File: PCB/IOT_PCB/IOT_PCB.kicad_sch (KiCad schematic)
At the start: 19 parts, among them J1 Screw_Terminal_01x02, J2 Screw_Terminal_01x02, J3 10155435-00011LF USB-C, U1 ESP32-S3-MINI-1, U2 BME280, U3 SCD41-D-R2, U4 ENS160-BGLM, U5 AMS1117-3.3, U6 AMS1117-1.8, U7 USBLC6-2SC6

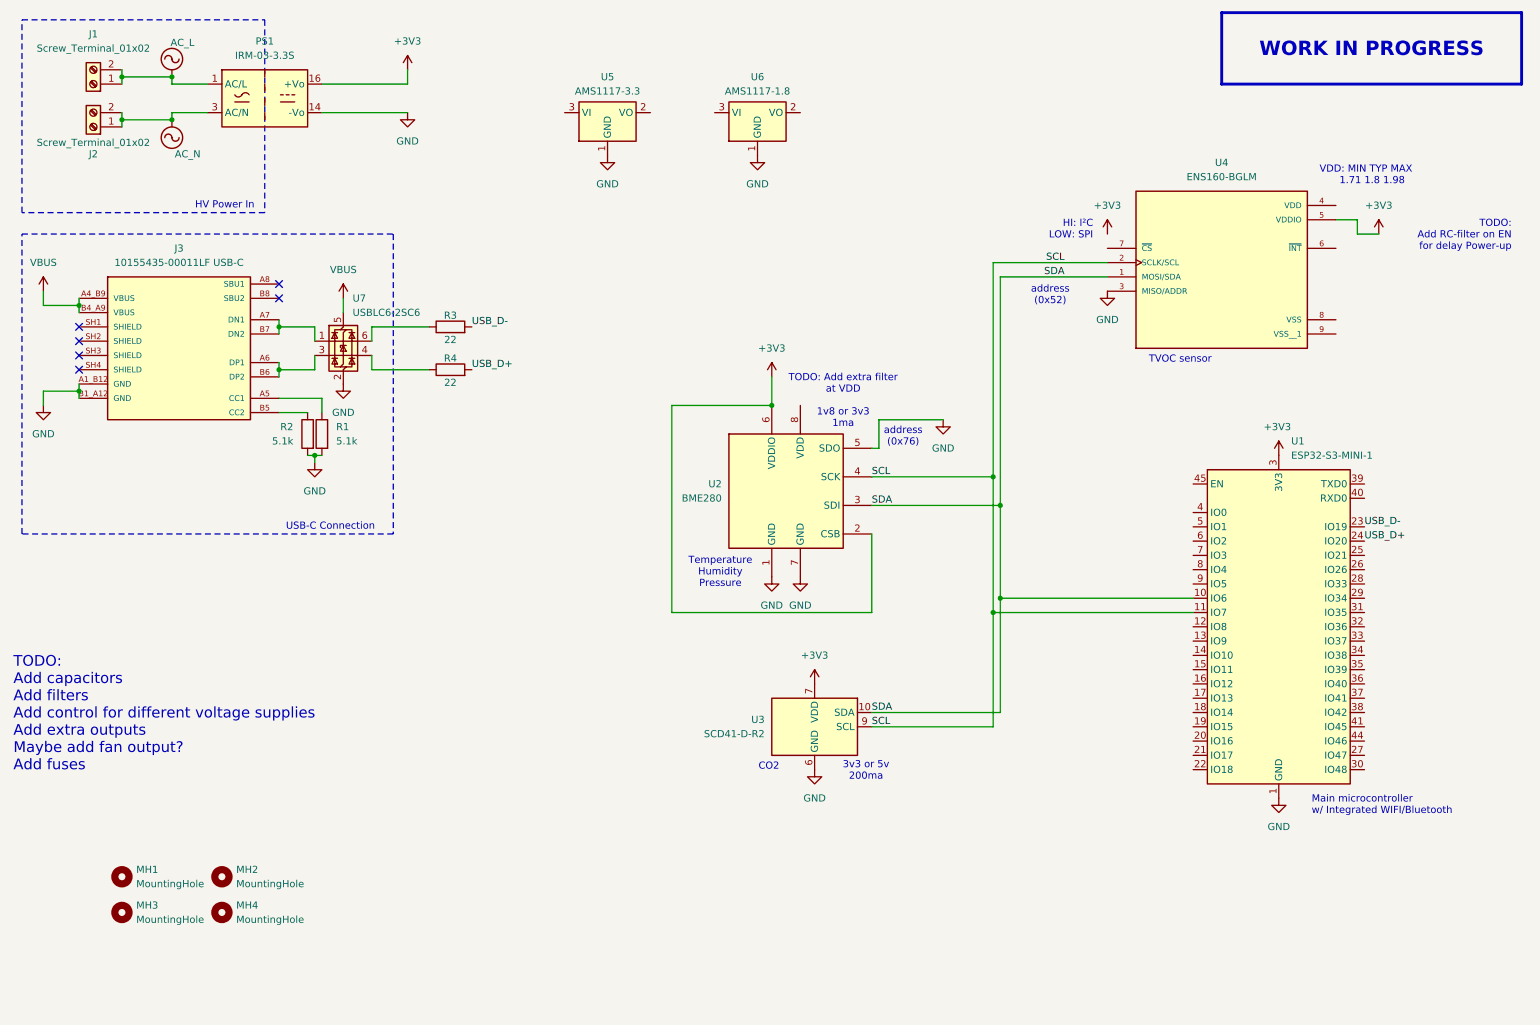
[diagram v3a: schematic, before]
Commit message: Power mannagement
Changed to beefier 5V supply instead of 3V3. Combined 5V supply with USB using diodes. Added caps and fuses.
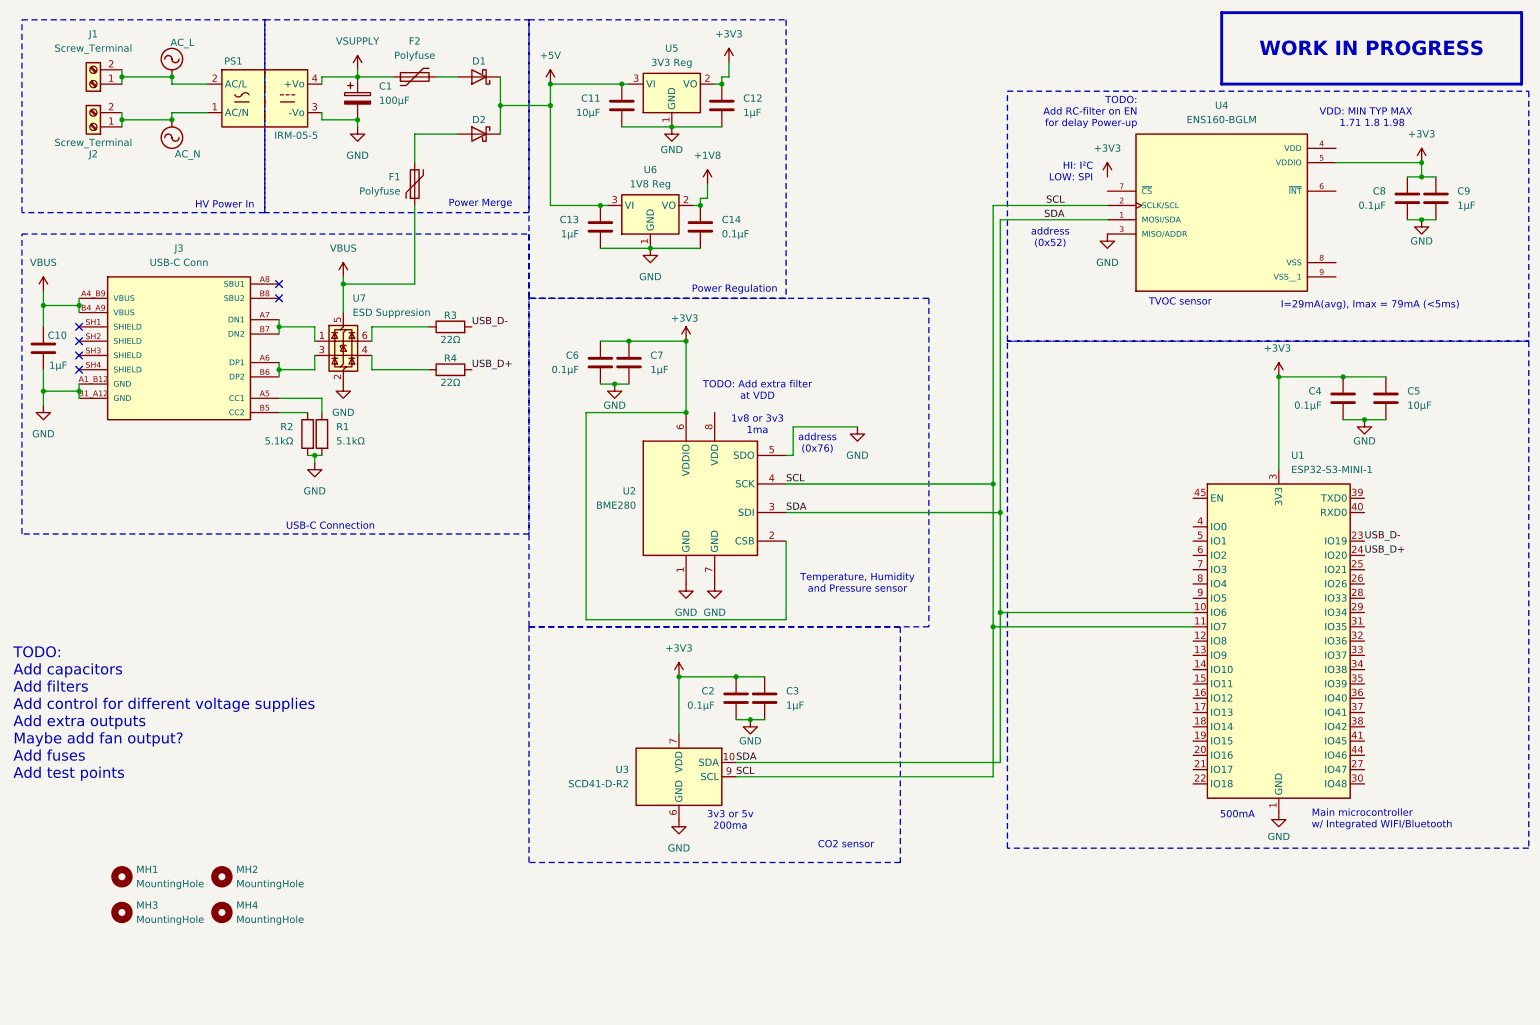
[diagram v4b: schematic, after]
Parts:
- removed PS1: IRM-03-3.3S, Converter_ACDC:Converter_ACDC_MeanWell_IRM-03-xx_SMD, symbol Converter_ACDC:IRM-03-3.3S
- removed U5: AMS1117-3.3, Package_TO_SOT_SMD:SOT-223-3_TabPin2, symbol Regulator_Linear:AMS1117-3.3
- removed U6: AMS1117-1.8, Package_TO_SOT_SMD:SOT-223-3_TabPin2, symbol Regulator_Linear:AMS1117-1.8
- added C1: 100µF, Capacitor_Tantalum_SMD:CP_EIA-3216-12_Kemet-S, symbol Device:C_Polarized
- added C10, C12, C13, C3, C7, C9: 1µF, Capacitor_SMD:C_0805_2012Metric_Pad1.18x1.45mm_HandSolder, symbol Device:C
- added C11, C5: 10µF, Capacitor_SMD:C_0805_2012Metric_Pad1.18x1.45mm_HandSolder, symbol Device:C
- added C14, C2, C4, C6, C8: 0.1µF, Capacitor_SMD:C_0603_1608Metric_Pad1.08x0.95mm_HandSolder, symbol Device:C
- added D1, D2: ~, symbol Device:D_Schottky
- added F1, F2: Polyfuse, Resistor_SMD:R_0805_2012Metric_Pad1.20x1.40mm_HandSolder, symbol Device:Polyfuse
- added PS1: IRM-05-5, Converter_ACDC:Converter_ACDC_MeanWell_IRM-05-xx_THT, symbol Converter_ACDC:IRM-05-5
- added U5: 3V3 Reg, Package_TO_SOT_THT:TO-220-3_Vertical, symbol Regulator_Linear:LM1117T-3.3
- added U6: 1V8 Reg, Package_TO_SOT_SMD:TO-252-3_TabPin2, symbol Regulator_Linear:LM1117DT-1.8
- J1, J2: value Screw_Terminal_01x02 -> Screw_Terminal
- J3: value 10155435-00011LF USB-C -> USB-C Conn
- R1, R2: value 5.1k -> 5.1kΩ; footprint Resistor_SMD:R_0805_2012Metric_Pad1.20x1.40mm_HandSolder -> Resistor_SMD:R_0603_1608Metric_Pad0.98x0.95mm_HandSolder
- R3, R4: value 22 -> 22Ω; footprint Resistor_SMD:R_0805_2012Metric_Pad1.20x1.40mm_HandSolder -> Resistor_SMD:R_0603_1608Metric_Pad0.98x0.95mm_HandSolder
- U7: value USBLC6-2SC6 -> ESD Suppresion
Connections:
- net +3V3: now also C12.1, C2.1, C3.1, C4.1, C5.1, C6.1, C7.1, C8.1, C9.1, U5.2 (VO)
- net AC_L: now also PS1.2 (AC/L)
- net AC_N: now also PS1.1 (AC/N)
- net GND: now also C1.2, C10.2, C11.2, C12.2, C13.2, C14.2, C2.2, C3.2, C4.2, C5.2, C6.2, C7.2, C8.2, C9.2, PS1.3 (-Vo), U5.1 (GND), U6.1 (GND)
- net VBUS: now also C10.1, F1.1
- new net: D1.2 (A), F2.2
- new net: D2.2 (A), F1.2
- new net +1V8: C14.1, U6.2 (VO)
- new net +5V: C11.1, C13.1, D1.1 (K), D2.1 (K), U5.3 (VI), U6.3 (VI)
- new net VSUPPLY: C1.1, F2.1, PS1.4 (+Vo)
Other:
- note added: "500mA"
- note added: "CO2 sensor"
- note added: "I=29mA(avg), Imax = 79mA (<5ms)"
- note added: "Power Merge"
- note added: "Power Regulation"
- note added: "TODO: Add capacitors Add filters Add control for different voltage supplies Add extra outputs Maybe add fan output? Add fuses Add test points"
- note added: "Temperature, Humidity and Pressure sensor"
- note removed: "CO2"
- note removed: "TODO: Add capacitors Add filters Add control for different voltage supplies Add extra outputs Maybe add fan output? Add fuses"
- note removed: "Temperature Humidity Pressure"
- moved on the sheet: U1, U2, U3, U4

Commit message: Changed Power Supply
Power supply changed from Mean Well to RECOM
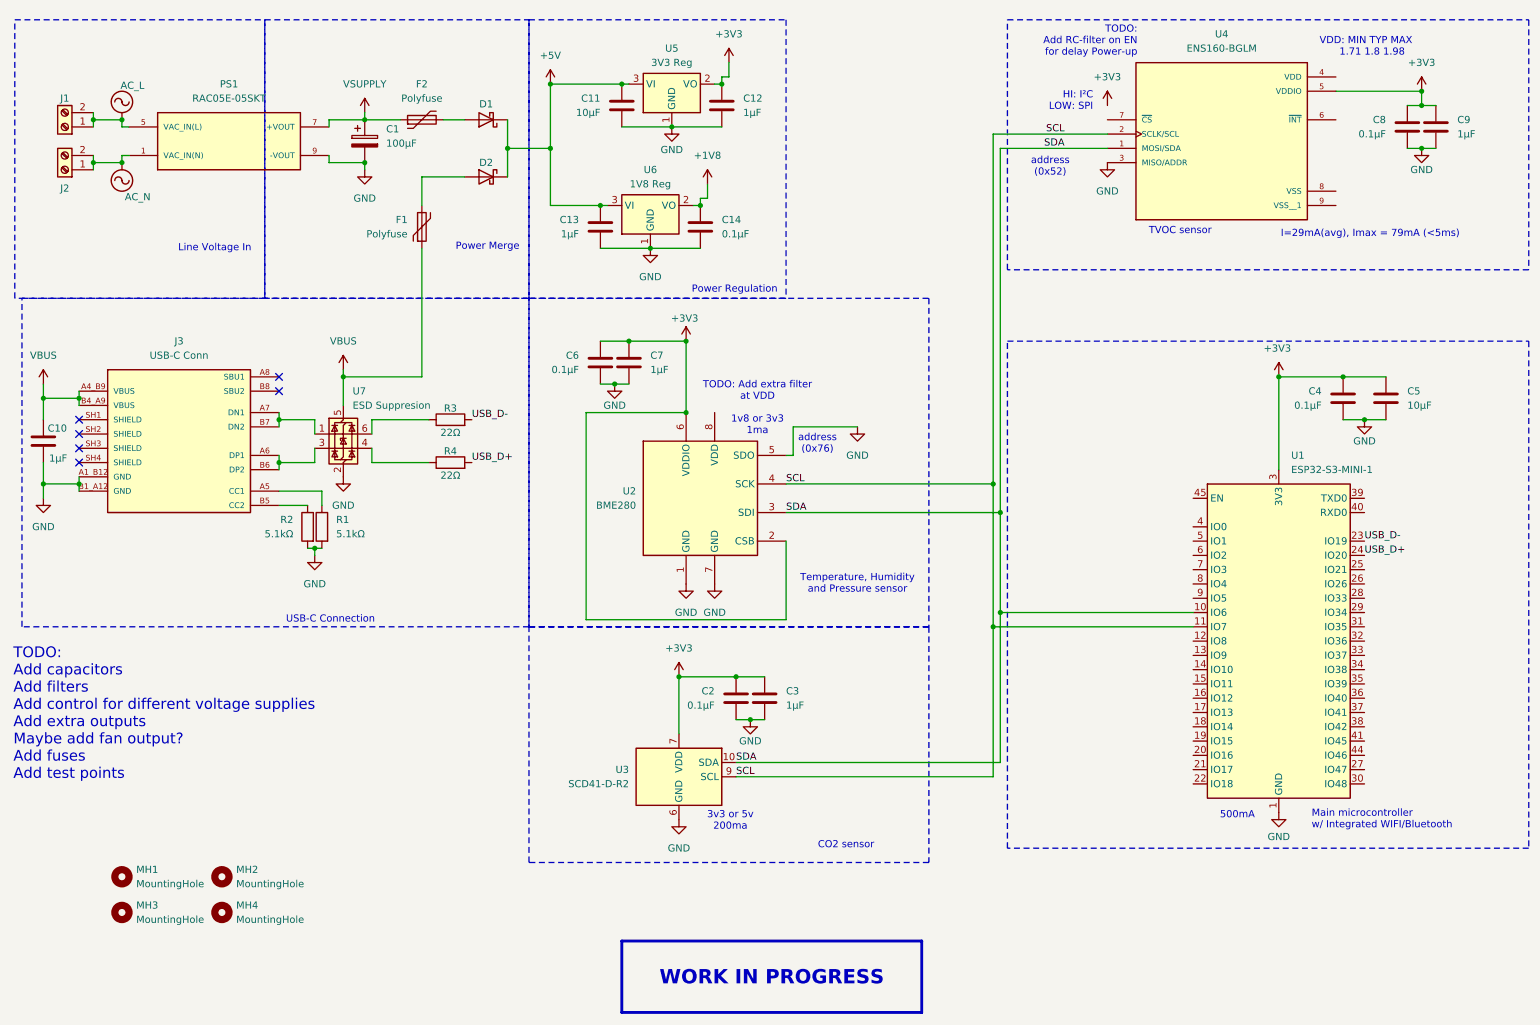
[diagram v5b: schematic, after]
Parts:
- removed PS1: IRM-05-5, Converter_ACDC:Converter_ACDC_MeanWell_IRM-05-xx_THT, symbol Converter_ACDC:IRM-05-5
- added PS1: RAC05E-05SKT, RAC05E_05SKT:CONV_RAC05E-05SKT, symbol RAC05E-05SKT:RAC05E-05SKT
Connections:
- net AC_L: now also PS1.5 (VAC_IN(L))
- net AC_N: now also PS1.1 (VAC_IN(N))
- net GND: now also PS1.9 (-VOUT)
- net VSUPPLY: now also PS1.7 (+VOUT)
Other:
- note added: "Line Voltage In"
- note removed: "HV Power In"
- moved on the sheet: C1, C10, C8, C9, D1, D2, F1, F2, J1, J2, J3, R1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

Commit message: Finalized Design (Rev A)
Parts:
- removed MH3, MH4: MountingHole, MountingHole:MountingHole_3.2mm_M3, symbol Mechanical:MountingHole
- removed U5: 3V3 Reg, Package_TO_SOT_THT:TO-220-3_Vertical, symbol Regulator_Linear:LM1117T-3.3
- removed U6: 1V8 Reg, Package_TO_SOT_SMD:TO-252-3_TabPin2, symbol Regulator_Linear:LM1117DT-1.8
- added C15: 10µF, Capacitor_SMD:C_0805_2012Metric_Pad1.18x1.45mm_HandSolder, symbol Device:C_Small
- added J4: SM06B-GHS-TB, Connector_JST:JST_GH_SM06B-GHS-TB_1x06-1MP_P1.25mm_Horizontal, symbol Connector_Generic_MountingPin:Conn_01x06_MountingPin
- added J5: ST GH 1.25MM 6 PIN CABLE, symbol Connector:Conn_01x06_Socket
- added J6: Screw_Terminal_01x04, TerminalBlock_MetzConnect:TerminalBlock_MetzConnect_Type101_RT01604HBWC_1x04_P5.08mm_Horizontal, symbol Connector:Screw_Terminal_01x04
- added R5, R6: 4.7kΩ, Resistor_SMD:R_0603_1608Metric_Pad0.98x0.95mm_HandSolder, symbol Device:R
- added TP1, TP2, TP3, TP5, TP6: ~, Connector_Pin:Pin_D1.0mm_L10.0mm, symbol Connector:TestPoint
- added U5: 3V3 Reg, Package_TO_SOT_SMD:TO-252-3_TabPin2, symbol Theo_Library:TLV76133KVUR
- added U6: 1V8 Reg, Package_TO_SOT_SMD:SOT-223-3_TabPin2, symbol Theo_Library:TLV76118DCYR
- D1, D2: footprint (none) -> Diode_SMD:D_0805_2012Metric_Pad1.15x1.40mm_HandSolder
- U1: MANUFACTURER Espressif -> Espressif Systems
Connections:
- net +1V8: now also U4.4 (VDD), C15.1, J6.2 (Pin_2), U6.2 (VO)
- net +3V3: now also U2.8 (VDD), U4.7 (~{CS}), J6.3 (Pin_3), R5.1, R6.1, U5.2 (VO)
- net +5V: now also J4.1 (Pin_1), J5.1 (Pin_1), J6.4 (Pin_4), U5.3 (VI), U6.3 (VI)
- net AC_L: now also J2.1 (Pin_1), J2.2 (Pin_2); no longer J1.1 (Pin_1), J1.2 (Pin_2)
- net AC_N: now also J1.1 (Pin_1), J1.2 (Pin_2); no longer J2.1 (Pin_1), J2.2 (Pin_2)
- net GND: now also J3.SH1 (SHIELD), J3.SH2 (SHIELD), J3.SH3 (SHIELD), J3.SH4 (SHIELD), U4.8 (VSS), U4.9 (VSS__1), C15.2, J4.2 (Pin_2), J4.5 (Pin_5), J5.2 (Pin_2), J5.5 (Pin_5), J6.1 (Pin_1), U5.1 (GND), U6.1 (GND)
- net SCL: now also J4.4 (Pin_4), J5.4 (Pin_4), R6.2, TP2.1
- net SDA: now also J4.3 (Pin_3), J5.3 (Pin_3), R5.2, TP1.1
- net VBUS: now also TP3.1
- net at R4.1, U7.4 (I/O2): now also TP6.1
- net at R3.1, U7.6 (I/O1): now also TP5.1
- net Fuse_VSUPPLY: now reaches D1.2 (A), F2.2
- net Fuse_VBUS: now reaches D2.2 (A), F1.2
- new net: J4.6 (Pin_6), J5.6 (Pin_6)
- no-connect marks 6 -> 3
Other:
- note added: "TODO: Add filters Add fan output? Add TP to U4_6"
- note removed: "TODO: Add capacitors Add filters Add control for different voltage supplies Add extra outputs Maybe add fan output? Add fuses Add test points"
- note removed: "TODO: Add extra filter at VDD"
- moved on the sheet: C8, C9, J1, J2, MH1, MH2, R3, R4
